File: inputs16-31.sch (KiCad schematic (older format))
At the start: 160 parts

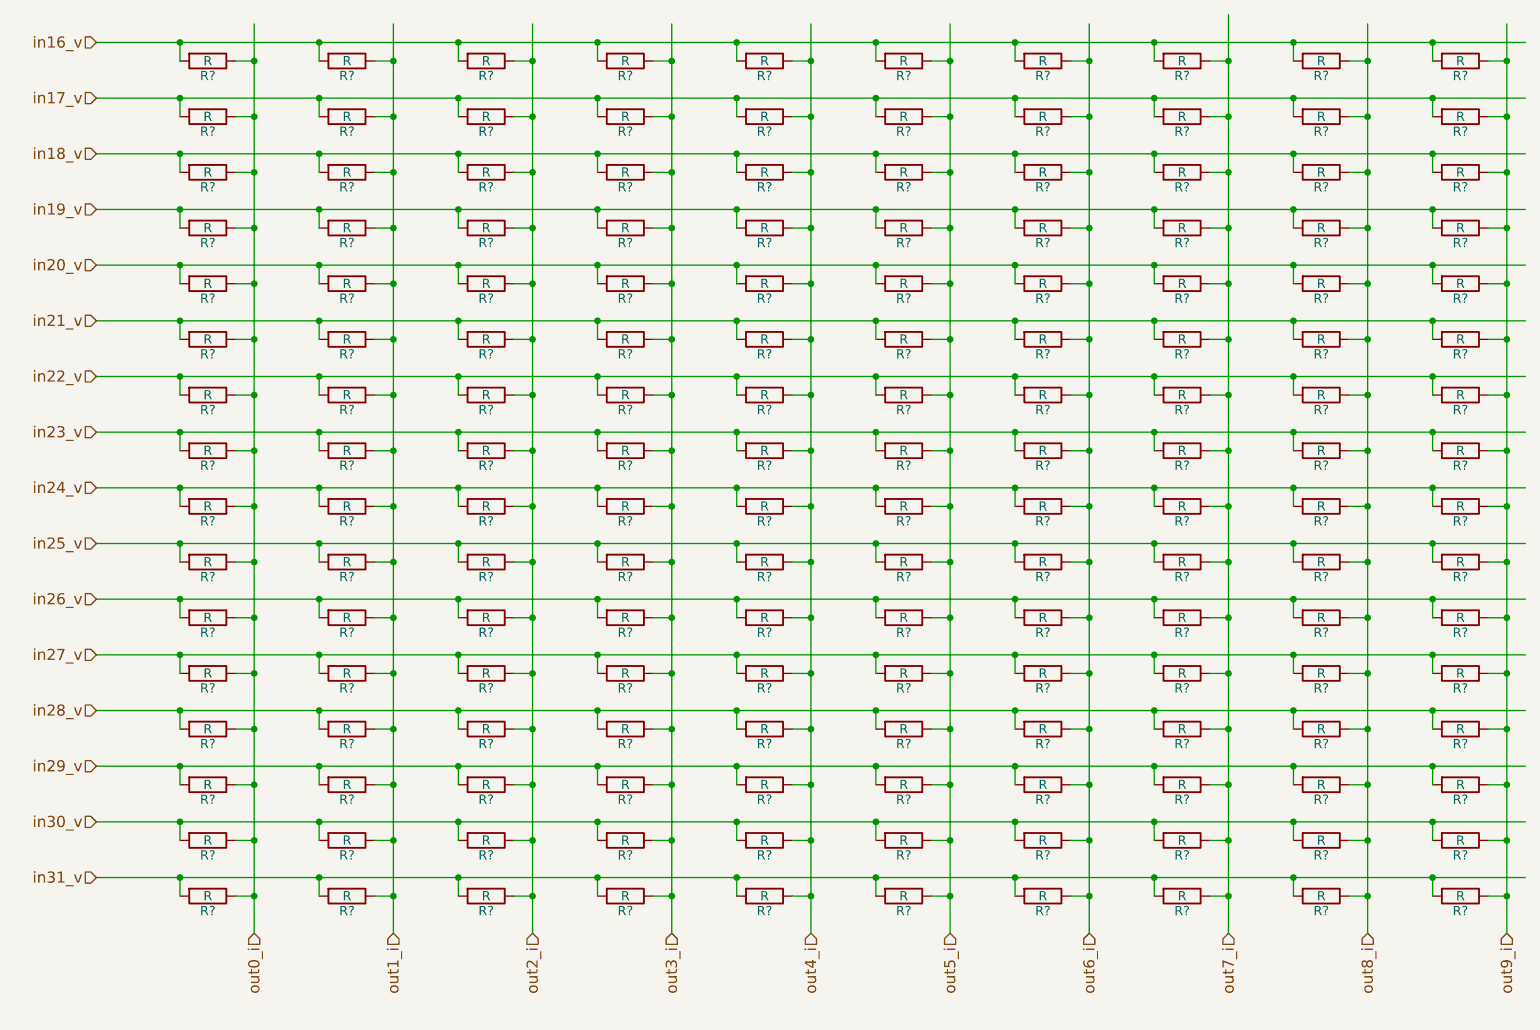
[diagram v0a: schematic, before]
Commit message: added 10k to respective position
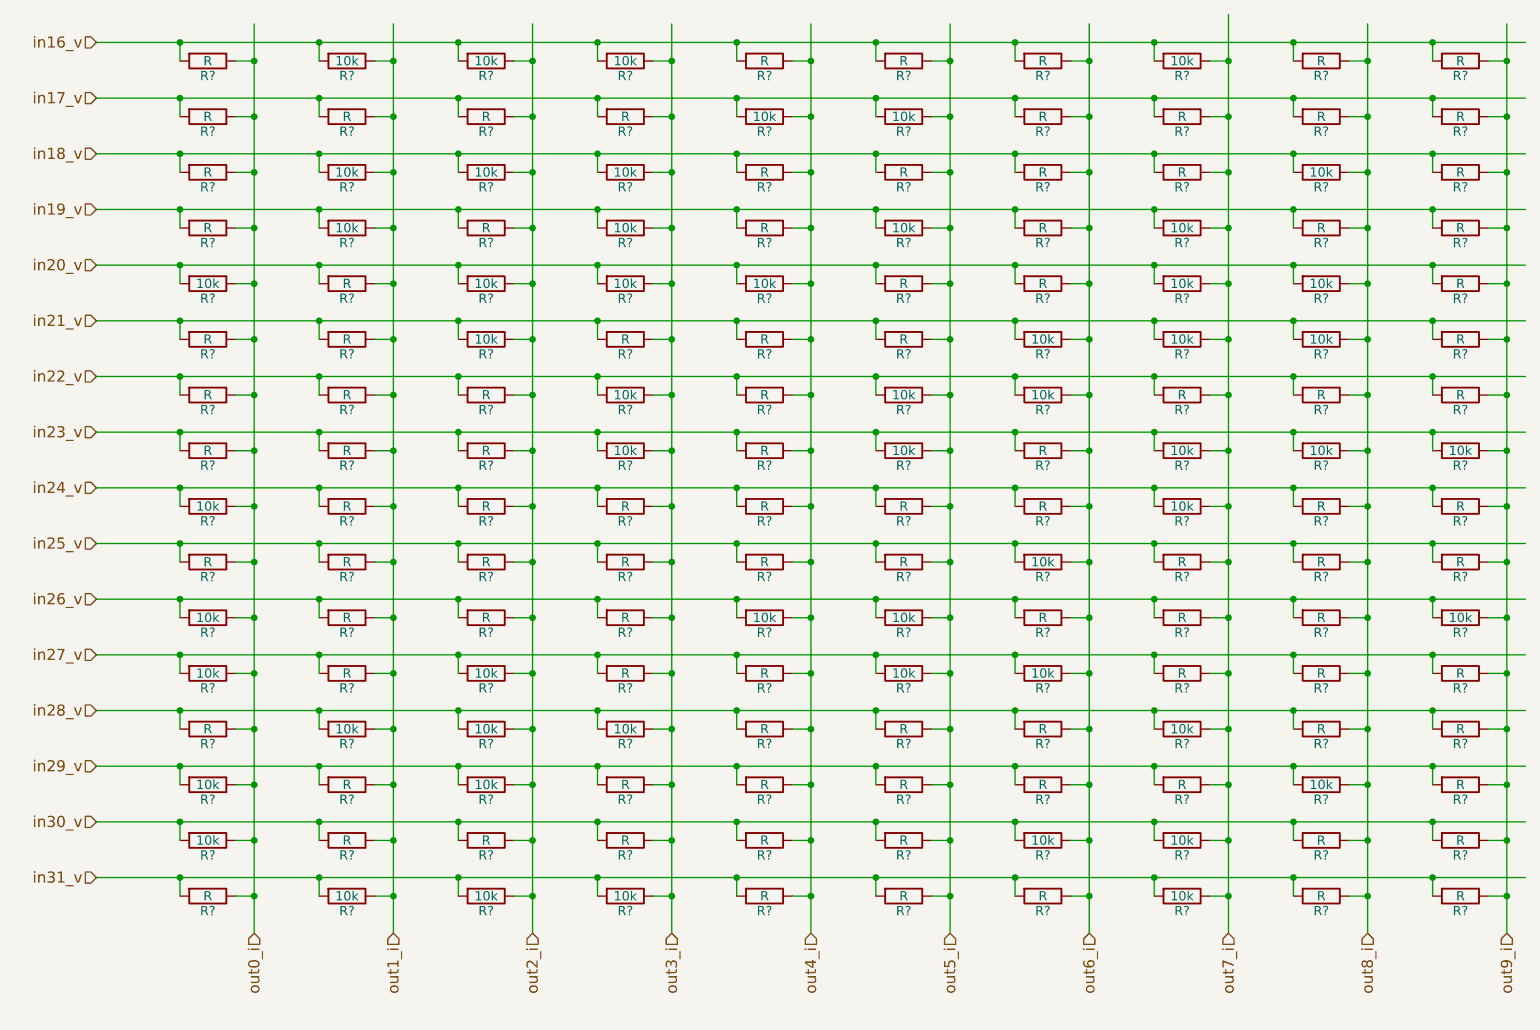
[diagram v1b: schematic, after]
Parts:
- R? (x57): value R -> 10k

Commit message: added resistor values for 16-31
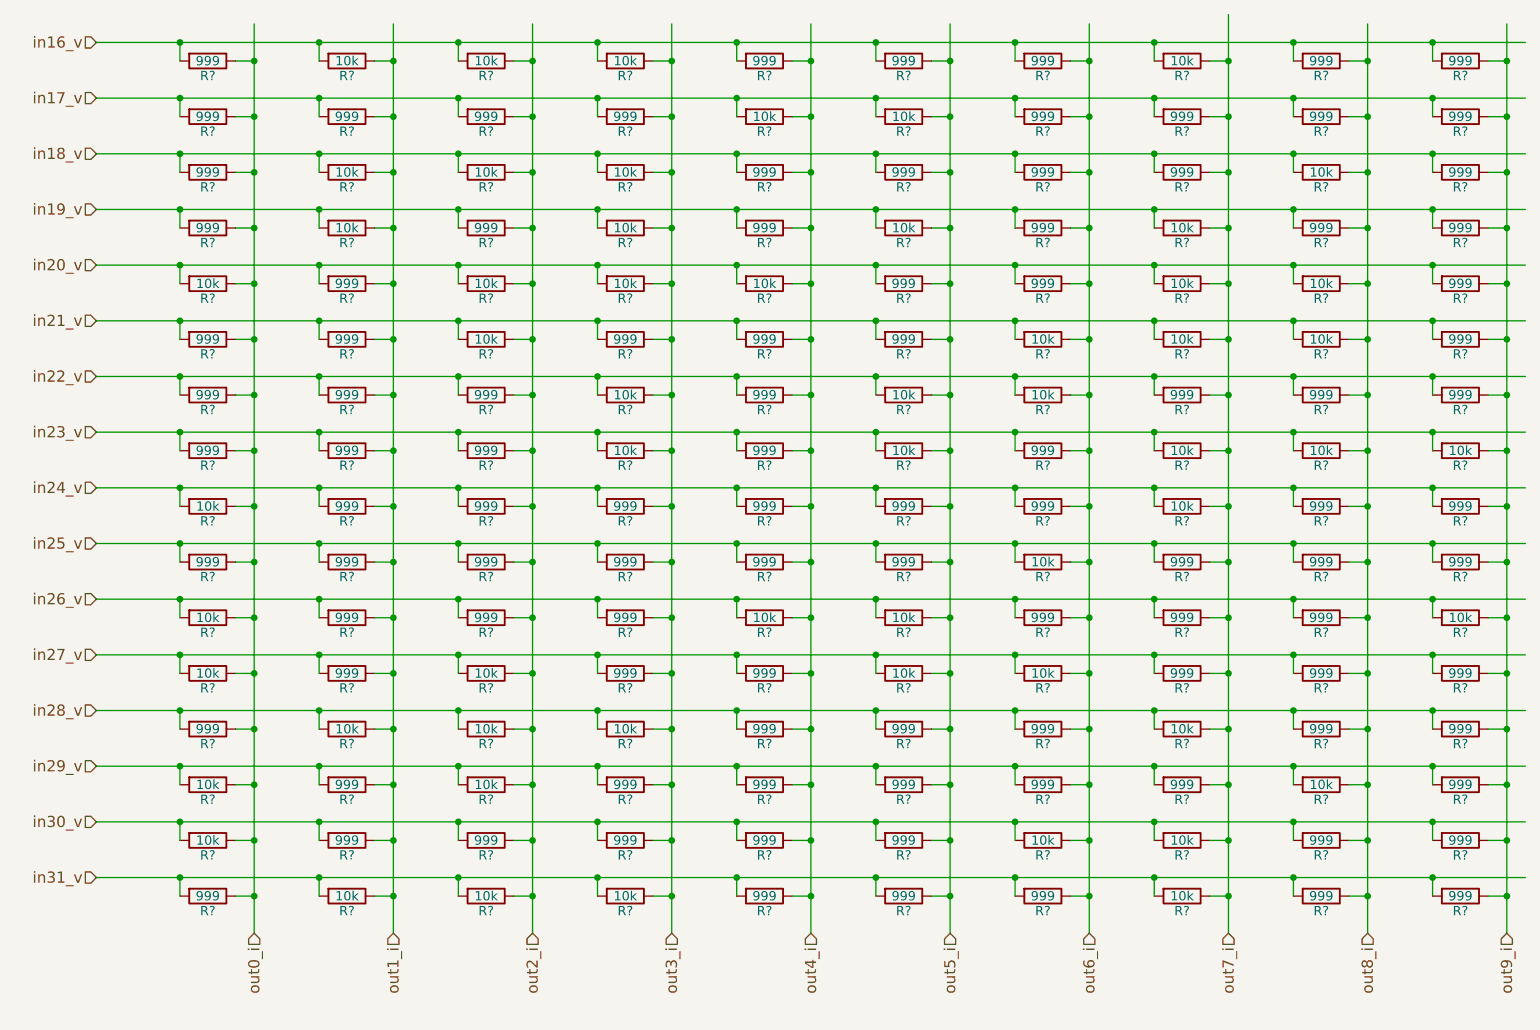
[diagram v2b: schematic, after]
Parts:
- R? (x103): value R -> 999

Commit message: added references for some resistors
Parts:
- gave numbers to parts that had none: 80

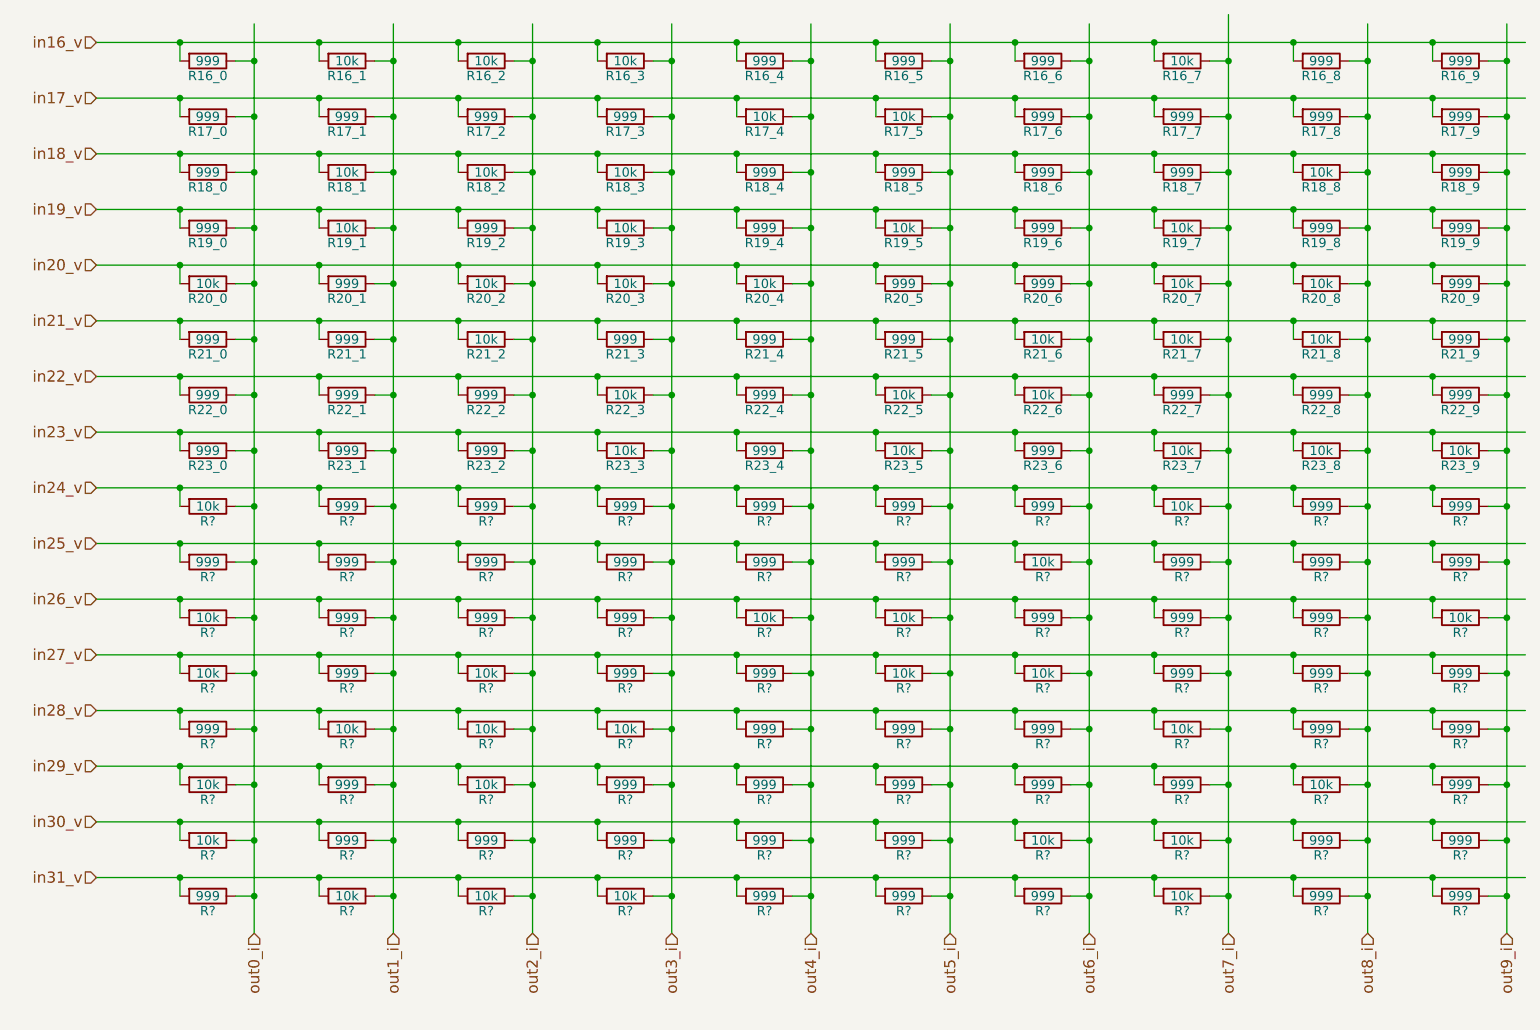
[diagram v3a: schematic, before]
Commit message: finished resistors0-31
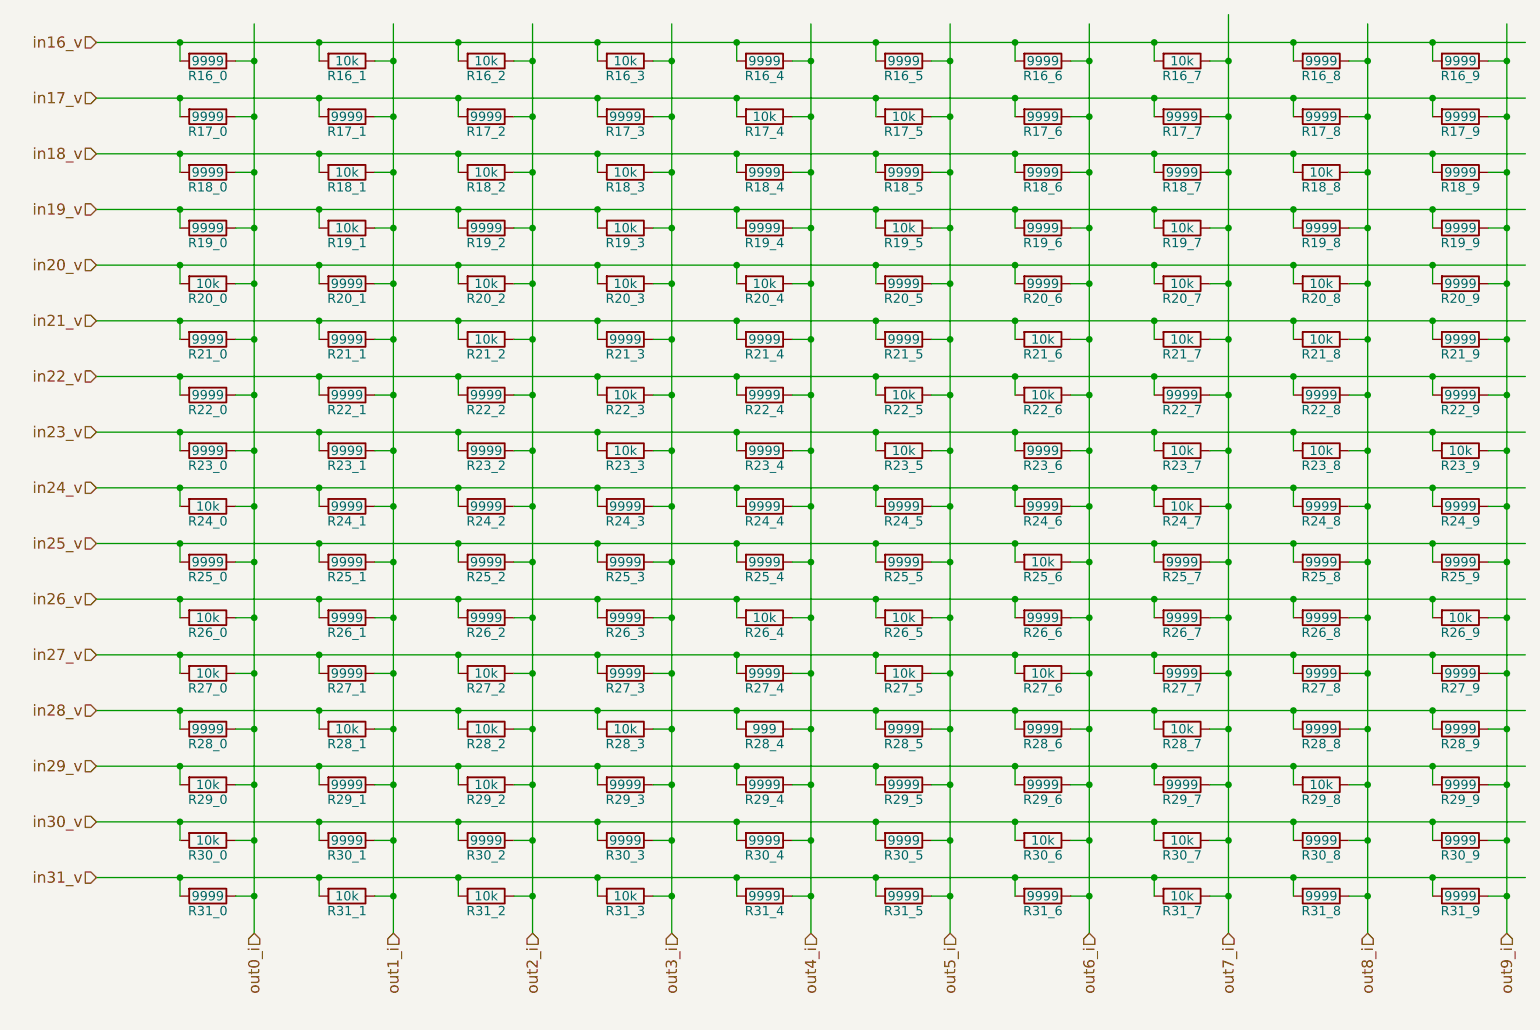
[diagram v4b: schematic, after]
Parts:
- R16_0, R16_4, R16_5, R16_6, R16_8, R16_9, R17_0, R17_1, R17_2, R17_3, R17_6, R17_7, R17_8, R17_9, R18_0, R18_4, R18_5, R18_6, R18_7, R18_9, R19_0, R19_2, R19_4, R19_6, R19_8, R19_9, R20_1, R20_5, R20_6, R20_9, R21_0, R21_1, R21_3, R21_4, R21_5, R21_9, R22_0, R22_1, R22_2, R22_4, R22_7, R22_8, R22_9, R23_0, R23_1, R23_2, R23_4, R23_6: value 999 -> 9999
- R24_1, R24_2, R24_3, R24_4, R24_5, R24_6, R24_8, R24_9, R25_0, R25_1, R25_2, R25_3, R25_4, R25_5, R25_7, R25_8, R25_9, R26_1, R26_2, R26_3, R26_6, R26_7, R26_8, R27_1, R27_3, R27_4, R27_7, R27_8, R27_9, R28_0, R28_5, R28_6, R28_8, R28_9, R29_1, R29_3, R29_4, R29_5, R29_6, R29_7, R29_9, R30_1, R30_2, R30_3, R30_4, R30_5, R30_8, R30_9, R31_0, R31_4, R31_5, R31_6, R31_8, R31_9: renamed from R?; value 999 -> 9999
- gave numbers to parts that had none: 26

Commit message: Added footprints, finished schematic, began PCB layout
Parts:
- R16_0, R16_1, R16_2, R16_3, R16_4, R16_5, R16_6, R16_7, R16_8, R16_9, R17_0, R17_1, R17_2, R17_3, R17_4, R17_5, R17_6, R17_7, R17_8, R17_9, R18_0, R18_1, R18_2, R18_3, R18_4, R18_5, R18_6, R18_7, R18_8, R18_9, R19_0, R19_1, R19_2, R19_3, R19_4, R19_5, R19_6, R19_7, R19_8, R19_9, R20_0, R20_1, R20_2, R20_3, R20_4, R20_5, R20_6, R20_7, R20_8, R20_9, R21_0, R21_1, R21_2, R21_3, R21_4, R21_5, R21_6, R21_7, R21_8, R21_9, R22_0, R22_1, R22_2, R22_3, R22_4, R22_5, R22_6, R22_7, R22_8, R22_9, R23_0, R23_1, R23_2, R23_3, R23_4, R23_5, R23_6, R23_7, R23_8, R23_9, R24_0, R24_1, R24_2, R24_3, R24_4, R24_5, R24_6, R24_7, R24_8, R24_9, R25_0, R25_1, R25_2, R25_3, R25_4, R25_5, R25_6, R25_7, R25_8, R25_9, R26_0, R26_1, R26_2, R26_3, R26_4, R26_5, R26_6, R26_7, R26_8, R26_9, R27_0, R27_1, R27_2, R27_3, R27_4, R27_5, R27_6, R27_7, R27_8, R27_9, R28_0, R28_1, R28_2, R28_3, R28_4, R28_5, R28_6, R28_7, R28_8, R28_9, R29_0, R29_1, R29_2, R29_3, R29_4, R29_5, R29_6, R29_7, R29_8, R29_9, R30_0, R30_1, R30_2, R30_3, R30_4, R30_5, R30_6, R30_7, R30_8, R30_9, R31_0, R31_1, R31_2, R31_3, R31_4, R31_5, R31_6, R31_7, R31_8, R31_9: footprint (none) -> Resistors_SMD:R_1206

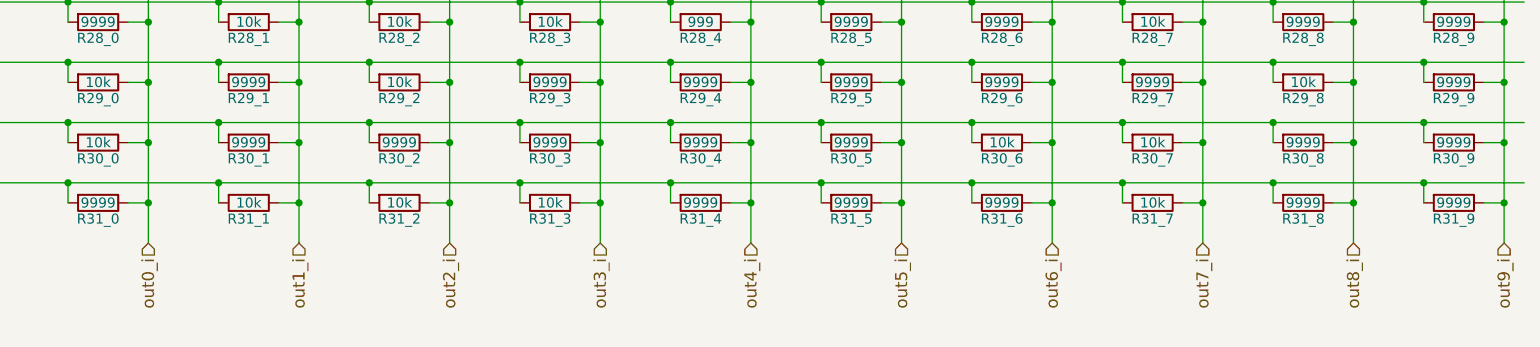
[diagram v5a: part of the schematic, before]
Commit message: fixed resistor schematic errors
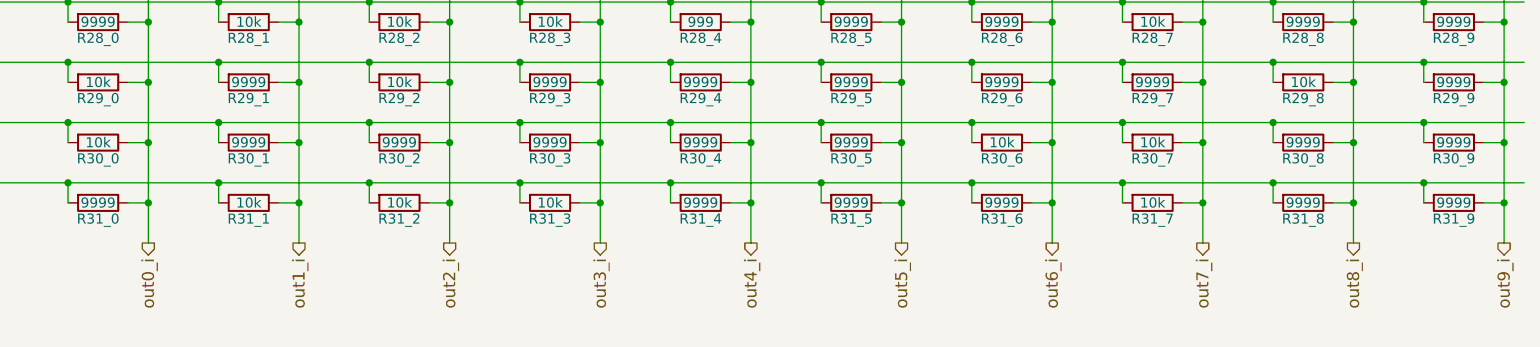
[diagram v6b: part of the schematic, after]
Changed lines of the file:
@@
 $Descr A4 11693 8268
 encoding utf-8
-Sheet 5 7
+Sheet 7 7
 Title ""
 Date ""
@@
 Text HLabel 2250 5650 0    60   Input ~ 0
 in31_v
-Text HLabel 3100 5950 3    60   Input ~ 0
+Text HLabel 3100 5950 3    60   Output ~ 0
 out0_i
-Text HLabel 3850 5950 3    60   Input ~ 0
+Text HLabel 3850 5950 3    60   Output ~ 0
 out1_i
-Text HLabel 4600 5950 3    60   Input ~ 0
+Text HLabel 4600 5950 3    60   Output ~ 0
 out2_i
-Text HLabel 5350 5950 3    60   Input ~ 0
+Text HLabel 5350 5950 3    60   Output ~ 0
 out3_i
-Text HLabel 6100 5950 3    60   Input ~ 0
+Text HLabel 6100 5950 3    60   Output ~ 0
 out4_i
-Text HLabel 6850 5950 3    60   Input ~ 0
+Text HLabel 6850 5950 3    60   Output ~ 0
 out5_i
-Text HLabel 7600 5950 3    60   Input ~ 0
+Text HLabel 7600 5950 3    60   Output ~ 0
 out6_i
-Text HLabel 8350 5950 3    60   Input ~ 0
+Text HLabel 8350 5950 3    60   Output ~ 0
 out7_i
-Text HLabel 9100 5950 3    60   Input ~ 0
+Text HLabel 9100 5950 3    60   Output ~ 0
 out8_i
-Text HLabel 9850 5950 3    60   Input ~ 0
+Text HLabel 9850 5950 3    60   Output ~ 0
 out9_i
 $Comp
